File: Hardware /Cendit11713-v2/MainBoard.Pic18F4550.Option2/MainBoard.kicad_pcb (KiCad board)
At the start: 2 copper layers, 86 parts, among them CON1 POWER_BUS, CON2 ICSP_CON, CON3 USB_CON, J1 RESET_CON, J2 SATA_PLUG _22P_SMT, J4 SATA_PLUG _22P_SMT, P1 DEBUG_HEADER_21P, P2 DEBUG_HEADER_21P, Q1 2N2222, U1 PIC18F4550-I/P, U3 PCF85263A, Y1 Crystal, Y2 32.768KHZ

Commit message: En CenditLab + Cendit11713: commit masivo
 - Trabajo en clases + fxml UI
 - Trabajo en main board option 2 + correccion tarjeta expansor Viking
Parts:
- C3: value 0.1uF -> 1uF; footprint Capacitors_SMD:C_0805_HandSoldering -> Capacitors_SMD:C_1206_HandSoldering
- moved C14 23.9 mm to (181.4, 129.8)
- moved C10 22.7 mm to (158.6, 129.5)
- moved C4 19.7 mm to (204.9, 132.3), turned to 270 degrees
- moved C13 19.1 mm to (178.8, 128.8)
- moved C9 17.3 mm to (161.2, 128.7)
- moved R46 16.5 mm to (157.4, 133.2)
- moved C3 15.5 mm to (202.0, 131.4), turned to 270 degrees
- moved JP1 10.8 mm to (230.5, 122.3), turned to 0 degrees
- moved CON3 9.13 mm to (221.3, 127.3)
- moved D3 8.84 mm to (217.4, 126.0), turned to 180 degrees
- moved L2 8.66 mm to (210.5, 130.8)
- moved D5 8.04 mm to (173.6, 67.6), turned to 180 degrees
- moved R2 6.58 mm to (216.7, 124.4), turned to 0 degrees
- moved R12 5.56 mm to (184.2, 143.1)
- moved JP2 5.54 mm to (185.3, 128.0), turned to 0 degrees
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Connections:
- CON1 pad 10: Net-(CON1-Pad10) -> (no net)
- CON1 pad 6: Net-(CON1-Pad6) -> (no net)
- CON1 pad 8: Net-(CON1-Pad8) -> (no net)
- J2 pad 2: /GND_PWR -> GNDPWR
- J2 pad 5: /VCC_3V -> /VDD_3V
- P2 pad 20: /GND_PWR -> GNDPWR
- R38 pad 2: /PB5 -> (no net)
- U3 pad 3: Net-(BT1-Pad1) -> (no net)
- U3 pad 7: Net-(U3-Pad7) -> (no net)
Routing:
- net GNDD: track 180.6 -> 629.8 mm, vias 6 -> 11
- net GNDPWR: track 40.5 -> 203.9 mm, vias 1 -> 2
- net /VDD_3V: track 19.7 -> 152.3 mm, vias 0 -> 2
- net /VCC_5V: track 21.6 -> 153.1 mm, vias 0 -> 3
- net /VPWR: track 9.55 -> 128.9 mm, vias 1 -> 2
- net VDD: track 79.3 -> 123.2 mm
- net Net-(CON3-Pad1): track 13.7 -> 3.26 mm
- net /USB_D-: track 38.5 -> 31.7 mm
- net /PE2: track 27.7 -> 34.3 mm
- net /PA4: track 30.6 -> 36.8 mm
- net /PC2: track 36.8 -> 42.9 mm
- net /PD0: track 39.7 -> 45.7 mm
- net /PA3: track 29.5 -> 35.3 mm
- net /PA5: track 28.4 -> 33.7 mm
- net /PE1: track 29.2 -> 34.0 mm
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- added copper zone on F.Cu, net GNDD

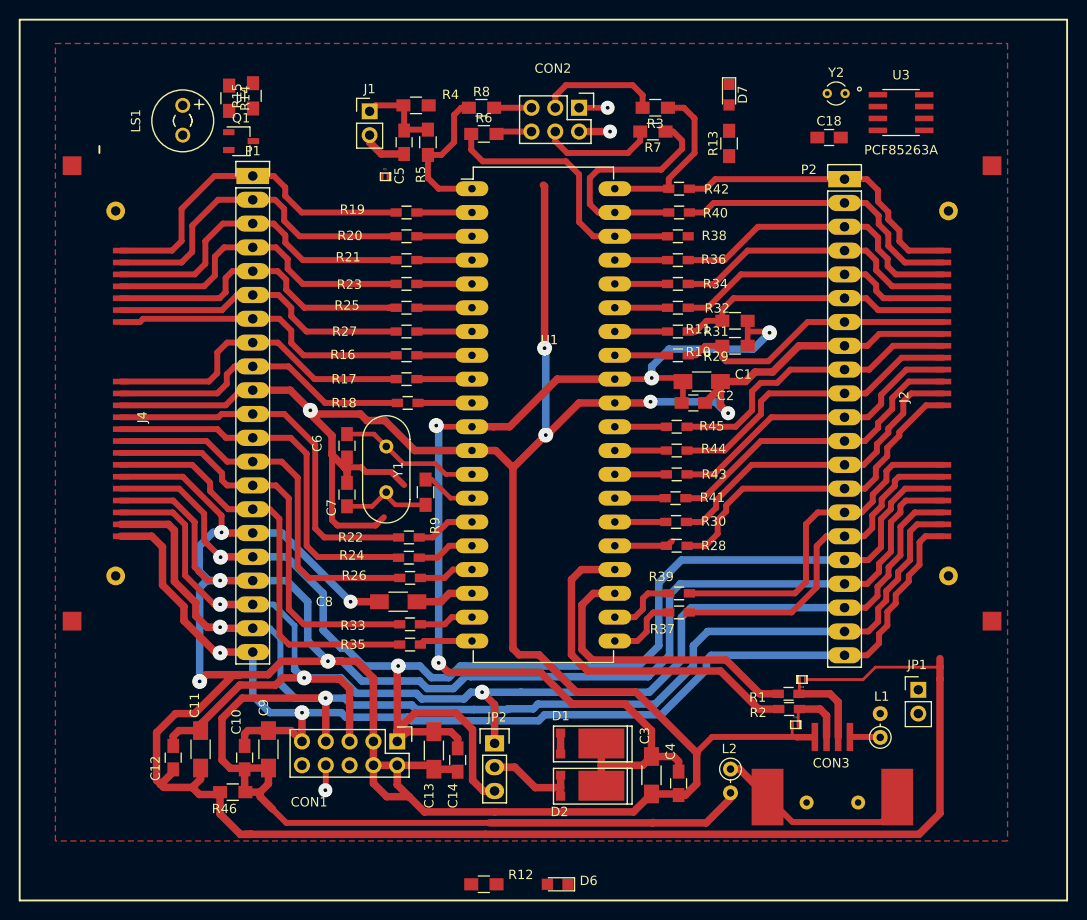
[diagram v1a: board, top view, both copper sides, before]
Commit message: En CenditLab + Cendit11713
  - Edicion de PCB tarjeta madre
  - Revision de PCB expansor Viking
  - Archivos gerber generados

  - Edicion de clases UI
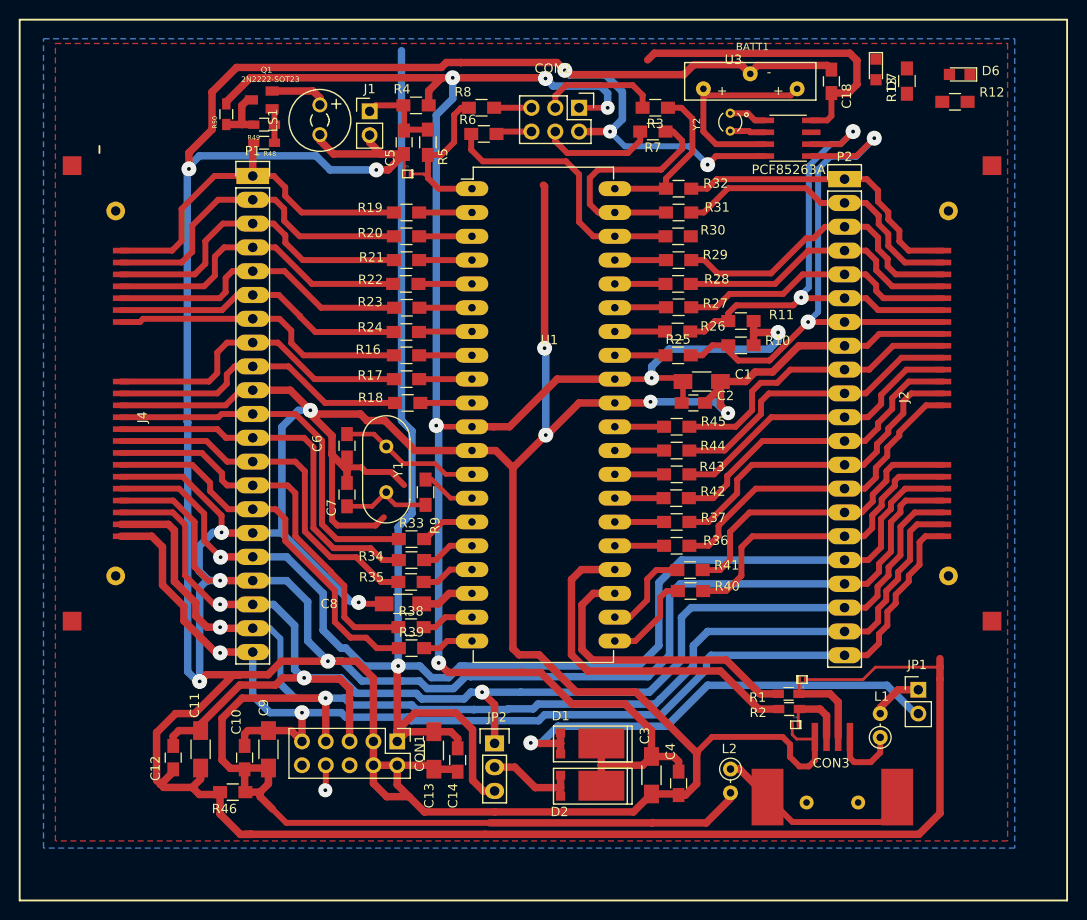
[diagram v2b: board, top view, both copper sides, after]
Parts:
- removed R14: 300, Resistors_SMD:R_0805_HandSoldering
- removed R15: 1k, Resistors_SMD:R_0805_HandSoldering
- added BATT1: BATT_HLD_VERT_CR2032, CenditFootprints:BATTERY_HOLDER_VERT_CR2032, F.Cu at (212.6, 57.4)
- added R48: 300, Resistors_SMD:R_0603_HandSoldering, F.Cu at (160.7, 63.9)
- added R49: 10k, Resistors_SMD:R_0603_HandSoldering, F.Cu at (160.7, 62.0)
- added R50: 1k, Resistors_SMD:R_0603_HandSoldering, F.Cu at (156.7, 60.9)
- CON1: footprint Pin_Headers:Pin_Header_Straight_2x05 -> Pin_Headers:Pin_Header_Straight_2x05_Pitch2.54mm
- Q1: value 2N2222 -> 2N2222-SOT23; footprint TO_SOT_Packages_SMD:TSOT-23 -> CenditFootprints:MMBT2222ALT1-SOT23
- R16, R17, R18, R19, R20, R21, R22, R23, R24, R25, R26, R27, R28, R29, R30, R31, R32, R33, R34, R35, R36, R37, R38, R39, R40, R41, R42, R43, R44, R45: footprint Resistors_SMD:R_0603_HandSoldering -> Resistors_SMD:R_0805_HandSoldering
- moved R12 97.5 mm to (234.4, 59.6)
- moved D6 96.5 mm to (234.9, 56.6)
- moved R38 50.5 mm to (176.4, 115.6)
- moved R34 40.9 mm to (176.4, 108.5)
- moved R40 40.4 mm to (206.2, 111.8), turned to 180 degrees
- moved R26 38.8 mm to (204.8, 84.1)
- moved R42 33.0 mm to (204.7, 101.9), turned to 180 degrees
- moved R30 30.5 mm to (204.9, 73.9), turned to 0 degrees
- moved R36 30.5 mm to (204.7, 106.9), turned to 180 degrees
- moved R25 29.4 mm to (204.9, 86.6), turned to 0 degrees
- moved R27 29.1 mm to (204.9, 81.5), turned to 0 degrees
- moved R39 29.1 mm to (176.4, 117.9), turned to 0 degrees
- moved R28 27.9 mm to (204.9, 79.0), turned to 0 degrees
- moved R22 27.1 mm to (175.8, 79.0), turned to 180 degrees
- moved R24 24.1 mm to (175.9, 84.1), turned to 180 degrees
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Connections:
- CON1 pad 10: (no net) -> Net-(CON1-Pad10)
- CON1 pad 6: (no net) -> Net-(CON1-Pad6)
- CON1 pad 8: (no net) -> Net-(CON1-Pad8)
- LS1 pad 1: Net-(LS1-Pad1) -> GNDD
- Q1 pad 3: GNDD -> Net-(Q1-Pad3)
- R22 pad 1: /PC0 -> /RA3
- R22 pad 2: /RC0 -> /PA3
- R23 pad 1: /RA3 -> /RA4
- R23 pad 2: /PA3 -> /PA4
- R24 pad 1: /PC1 -> /RA5
- R24 pad 2: /RC1 -> /PA5
- R25 pad 1: /RA4 -> /RB0
- R25 pad 2: /PA4 -> /PB0
- R26 pad 1: /PC2 -> /RB1
- R26 pad 2: /RC2 -> /PB1
- R27 pad 1: /RA5 -> /RB2
- R27 pad 2: /PA5 -> /PB2
- R28 pad 1: /MISO -> /RB3
- R28 pad 2: /RC6 -> /PB3
- R29 pad 1: /RB0 -> /RB4
- R29 pad 2: /PB0 -> /PB4
- R30 pad 1: /MOSI -> /LVP
- R30 pad 2: /RC7 -> /PB5
- R31 pad 1: /RB1 -> /PGC
- R31 pad 2: /PB1 -> /PB6
- R32 pad 1: /RB2 -> /PGD
- R32 pad 2: /PB2 -> /PB7
- R33 pad 1: /PD0 -> /PC0
- R33 pad 2: /RD0 -> /RC0
- R34 pad 1: /RB3 -> /PC1
- R34 pad 2: /PB3 -> /RC1
- R35 pad 1: /PD1 -> /PC2
- R35 pad 2: /RD1 -> /RC2
- R36 pad 1: /RB4 -> /MISO
- R36 pad 2: /PB4 -> /RC6
- R37 pad 1: //RST_KEY -> /MOSI
- R37 pad 2: /RD2 -> /RC7
- R38 pad 1: /LVP -> /PD0
- R38 pad 2: (no net) -> /RD0
- R39 pad 1: //RST_GPIB -> /PD1
- R39 pad 2: /RD3 -> /RD1
- R40 pad 1: /PGC -> //RST_KEY
- R40 pad 2: /PB6 -> /RD2
- R41 pad 1: //RST_LAN -> //RST_GPIB
- R41 pad 2: /RD4 -> /RD3
- R42 pad 1: /PGD -> //RST_LAN
- R42 pad 2: /PB7 -> /RD4
- U3 pad 3: (no net) -> Net-(BATT1-Pad1)
- U3 pad 7: (no net) -> Net-(U3-Pad7)
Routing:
- net GNDD: track 629.8 -> 850.2 mm, vias 11 -> 15
- net /VDD_3V: track 152.3 -> 252.4 mm
- net VDD: track 123.2 -> 210.2 mm, vias 5 -> 7
- net Net-(D1-Pad2): track 2.25 -> 50.6 mm, vias 0 -> 1
- net /PB0: track 30.8 -> 61.8 mm, vias 0 -> 2
- net /PB1: track 31.2 -> 56.4 mm, vias 0 -> 2
- net Net-(BATT1-Pad1): track 0.00 -> 22.5 mm
- net Net-(Q1-Pad3): track 0.00 -> 6.25 mm
- net Net-(LS1-Pad2): track 0.00 -> 6.16 mm
- net /USB_VBUS: track 0.00 -> 5.49 mm
- net Net-(CON3-Pad1): track 3.26 -> 7.77 mm
- net //RST_GPIB: track 37.5 -> 33.1 mm
- net Net-(U3-Pad1): track 0.00 -> 4.01 mm
- net /PD1: track 45.5 -> 41.6 mm
- net Net-(U3-Pad2): track 0.00 -> 3.75 mm
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- added copper zone on B.Cu, net GNDD

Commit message: Trabajo en CenditLab + Cendit11713
  - Diseño + codigo UI
  - PCBs tarjeta madre + puertos Viking
  - Se generan Gerber para solicitud de prototipos PCB
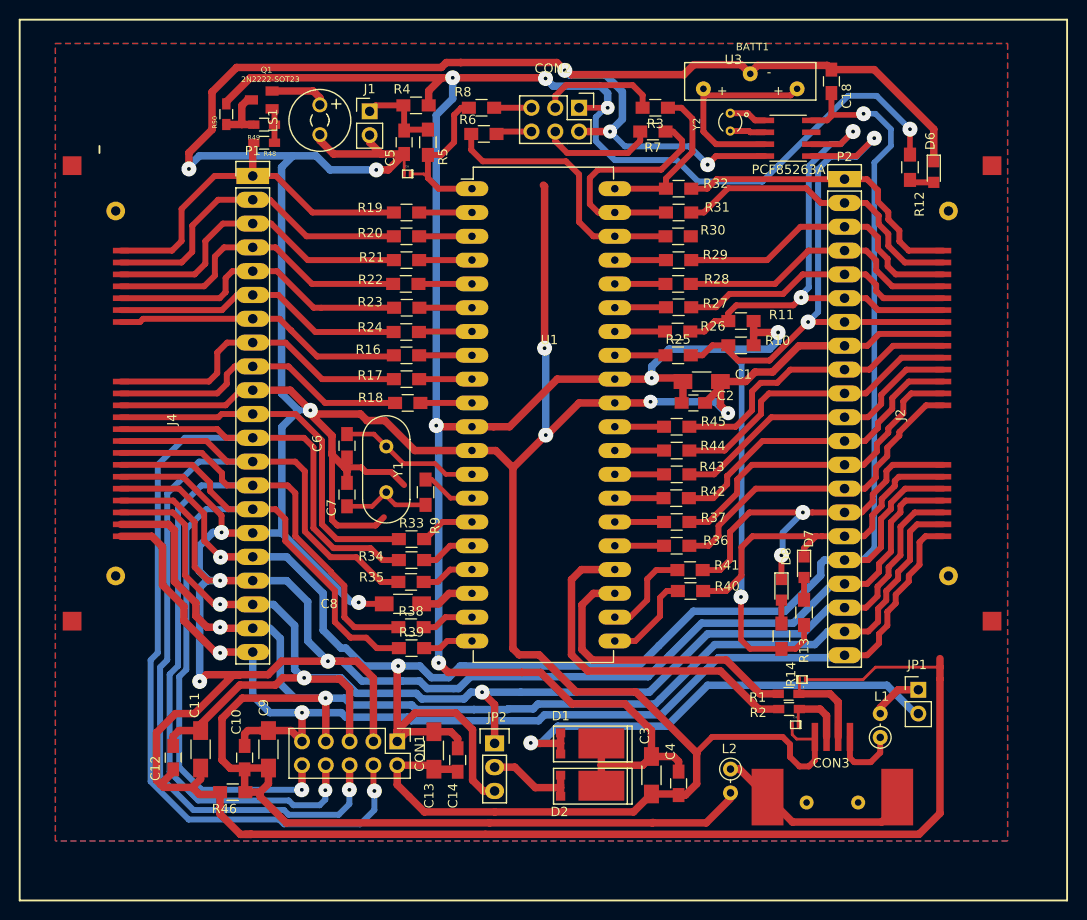
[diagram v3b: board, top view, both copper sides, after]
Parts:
- added D8: LED, LEDs:LED_0805, F.Cu at (215.9, 111.6)
- added R14: 300, Resistors_SMD:R_0805_HandSoldering, F.Cu at (215.9, 116.6)
- moved R13 57.7 mm to (218.3, 114.0)
- moved D7 53.7 mm to (218.3, 109.2)
- moved D6 10.8 mm to (232.2, 67.1), turned to 270 degrees
- moved R12 8.48 mm to (229.6, 66.5), turned to 270 degrees
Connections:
- CON1 pad 10: Net-(CON1-Pad10) -> /PD1
- CON1 pad 4: GNDD -> /PC1
- CON1 pad 6: Net-(CON1-Pad6) -> /PC2
- CON1 pad 8: Net-(CON1-Pad8) -> /PD0
- D7 pad 1: GNDD -> //RST_KEY
- R13 pad 1: /PB4 -> VDD
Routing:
- net VDD: track 210.2 -> 298.8 mm, vias 7 -> 9
- net /PC1: track 40.5 -> 117.2 mm, vias 0 -> 1
- net /PC2: track 41.1 -> 108.6 mm, vias 0 -> 1
- net /PD0: track 43.4 -> 102.8 mm, vias 0 -> 1
- net /PD1: track 41.6 -> 92.5 mm, vias 0 -> 1
- net /VDD_3V: track 252.4 -> 211.0 mm, vias 2 -> 3
- net GNDD: track 850.2 -> 826.7 mm
- net //RST_GPIB: track 33.1 -> 41.2 mm, vias 0 -> 2
- net //RST_KEY: track 34.0 -> 36.7 mm
- net Net-(CON1-Pad8): track 2.69 -> 0.00 mm, vias 1 -> 0
- net Net-(D6-Pad2): track 0.00 -> 2.65 mm
- net Net-(D8-Pad2): track 0.00 -> 2.50 mm
- net Net-(D7-Pad2): track 0.00 -> 2.38 mm
- net GNDPWR: track 203.9 -> 202.6 mm
- net /VCC_5V: track 153.1 -> 152.0 mm
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
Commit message: En Cendit11713 + CenditLab respaldo
  - Se revisan tarjetas
  - Correccion en PCB GPIB
  - Se inicia tarjeta madre en una pieza (MainBoard.OnePiece)
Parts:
- C8: value 1uF -> 0.1uF
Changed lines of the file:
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@@
       (effects (font (size 1 1) (thickness 0.15)))
     )
-    (fp_text value 1uF (at -4.826 0) (layer F.Fab)
+    (fp_text value 0.1uF (at -4.826 0) (layer F.Fab)
       (effects (font (size 1 1) (thickness 0.15)))
     )
@@
       (effects (font (size 1 1) (thickness 0.15)))
     )
-    (fp_text value POWER_BUS (at 1.27 12.55 270) (layer F.Fab)
+    (fp_text value POWER_BUS (at -2.0828 4.9784 360) (layer F.Fab)
       (effects (font (size 1 1) (thickness 0.15)))
     )
@@
   (segment (start 155.829 93.218) (end 145.415 93.218) (width 0.635) (layer F.Cu) (net 43))
   (segment (start 156.1719 92.8751) (end 155.829 93.218) (width 0.635) (layer F.Cu) (net 43))
-  (segment (start 159.4866 95.4151) (end 152.2349 95.4151) (width 0.635) (layer B.Cu) (net 44) (status 400000))
+  (segment (start 159.4866 95.4151) (end 152.2349 95.4151) (width 0.635) (layer B.Cu) (net 44))
   (segment (start 149.352 100.838) (end 149.352 118.364) (width 0.635) (layer B.Cu) (net 44))
   (segment (start 149.352 118.364) (end 148.59 119.126) (width 0.635) (layer B.Cu) (net 44))
@@
   (segment (start 170.942 136.652) (end 172.466 135.128) (width 0.635) (layer B.Cu) (net 44))
   (segment (start 172.466 135.128) (end 172.466 133.096) (width 0.635) (layer B.Cu) (net 44))
-  (segment (start 172.3644 132.9944) (end 172.3644 130.3528) (width 0.635) (layer F.Cu) (net 44) (status 800000))
+  (segment (start 172.3644 132.9944) (end 172.3644 130.3528) (width 0.635) (layer F.Cu) (net 44))
   (via (at 172.466 133.096) (size 1.6) (drill 0.4) (layers F.Cu B.Cu) (net 44))
   (segment (start 172.3644 132.9944) (end 172.466 133.096) (width 0.635) (layer F.Cu) (net 44))
@@
   (segment (start 156.6291 95.4151) (end 159.4866 95.4151) (width 0.635) (layer F.Cu) (net 44))
   (segment (start 155.702 94.488) (end 156.6291 95.4151) (width 0.635) (layer F.Cu) (net 44))
-  (segment (start 159.4866 97.9551) (end 153.7589 97.9551) (width 0.635) (layer B.Cu) (net 45) (status 400000))
+  (segment (start 159.4866 97.9551) (end 153.7589 97.9551) (width 0.635) (layer B.Cu) (net 45))
   (segment (start 169.8244 132.9436) (end 169.799 132.969) (width 0.8) (layer F.Cu) (net 45))
   (via (at 169.799 132.969) (size 1.6) (drill 0.4) (layers F.Cu B.Cu) (net 45))
@@
   (segment (start 156.7561 97.9551) (end 154.559 95.758) (width 0.635) (layer F.Cu) (net 45))
   (segment (start 158.0388 97.9551) (end 159.4866 97.9551) (width 0.635) (layer F.Cu) (net 45))
-  (segment (start 159.4866 100.4951) (end 154.0129 100.4951) (width 0.635) (layer B.Cu) (net 46) (status 400000))
+  (segment (start 159.4866 100.4951) (end 154.0129 100.4951) (width 0.635) (layer B.Cu) (net 46))
   (segment (start 167.2844 132.969) (end 167.2336 133.0198) (width 0.635) (layer F.Cu) (net 46))
   (via (at 167.2336 133.0198) (size 1.5) (drill 0.4) (layers F.Cu B.Cu) (net 46))
@@
   (segment (start 154.051 97.028) (end 156.21 99.187) (width 0.635) (layer F.Cu) (net 46))
   (segment (start 158.5595 100.4951) (end 159.4866 100.4951) (width 0.635) (layer F.Cu) (net 46))
-  (segment (start 159.4866 103.0351) (end 154.5209 103.0351) (width 0.635) (layer B.Cu) (net 47) (status 400000))
+  (segment (start 159.4866 103.0351) (end 154.5209 103.0351) (width 0.635) (layer B.Cu) (net 47))
   (segment (start 164.7444 132.9436) (end 164.719 132.969) (width 0.8) (layer F.Cu) (net 47))
   (via (at 164.719 132.969) (size 1.6) (drill 0.4) (layers F.Cu B.Cu) (net 47))
